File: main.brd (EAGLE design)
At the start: 78 x 235 mm, 116 parts, among them IC10 FGPMMOPA6H, IC2 25LC1024-I/P, IC6 MPL3115A2LGA, IC7 FXAS21000, IC8 ADXL343BCCZ, Q1 12MHz, Q2 MCP9700A-E/TO, Q3 FQP7P06, Q4 MCP9700A-E/TO, U1 ATMEGA1284P-PU, U2 LT3570EFEPBF, U3 TL431BQLP, X1 132134RP

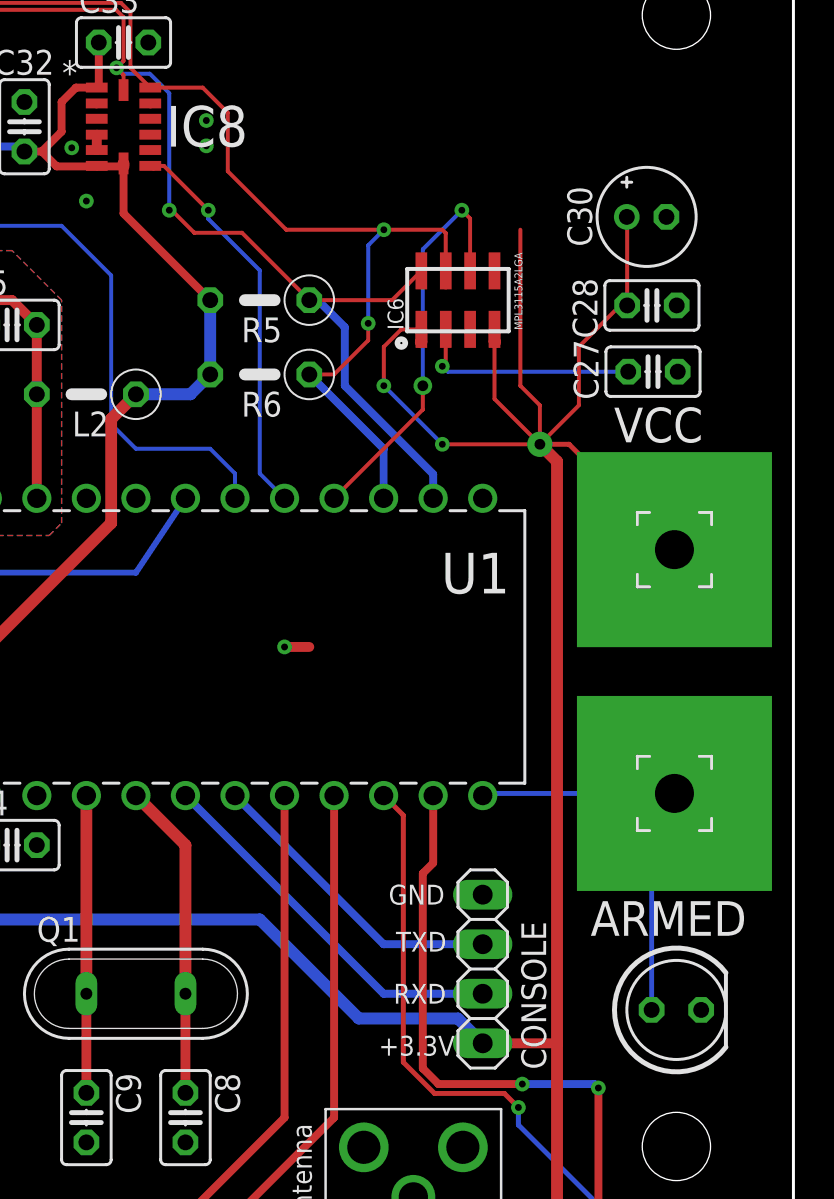
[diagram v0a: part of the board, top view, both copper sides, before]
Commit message: Changed armed sense so that the pin is pulled low when armed and added resistor for armed LED.
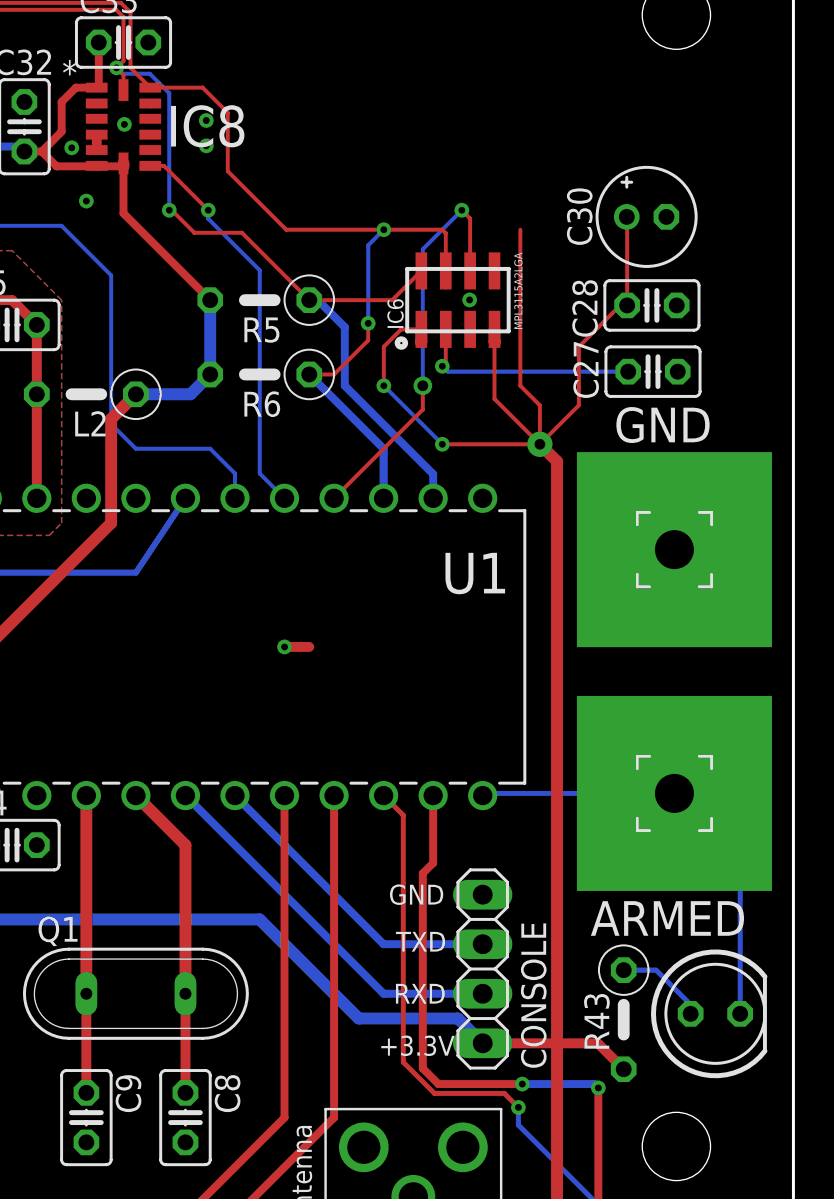
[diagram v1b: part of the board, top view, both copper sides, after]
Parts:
- added R43: 2K2Ω, rcl:0207/5V
- moved ARMED 2.01 mm to (74.0, 177.8)
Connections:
- new net N$33: ARMED.A, R43.1
- net ARMED_SENSE: now also ARMED.K; no longer ARMED.A
- net GND: now also PAD1.1; no longer ARMED.K
- net VCC: now also R43.2; no longer PAD1.1
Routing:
- net VCC: track 500.9 -> 495.7 mm
- net N$33: track 0.00 -> 4.63 mm
- net ARMED_SENSE: track 21.5 -> 22.6 mm
- net GND: vias 38 -> 40
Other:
- board text removed: "VCC"
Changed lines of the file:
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@@
 <?xml version="1.0" encoding="utf-8"?>
 <!DOCTYPE eagle SYSTEM "eagle.dtd">
-<eagle version="8.6.0">
+<eagle version="8.5.1">
 <drawing>
 <settings>
@@
 <grid distance="1" unitdist="mm" unit="mm" style="lines" multiple="1" display="no" altdistance="0.1" altunitdist="mm" altunit="mm"/>
 <layers>
-<layer number="1" name="Top" color="4" fill="1" visible="no" active="yes"/>
+<layer number="1" name="Top" color="4" fill="1" visible="yes" active="yes"/>
 <layer number="2" name="Route2" color="1" fill="3" visible="no" active="no"/>
 <layer number="3" name="Route3" color="4" fill="3" visible="no" active="no"/>
@@
 <layer number="17" name="Pads" color="2" fill="1" visible="yes" active="yes"/>
 <layer number="18" name="Vias" color="2" fill="1" visible="yes" active="yes"/>
-<layer number="19" name="Unrouted" color="6" fill="1" visible="no" active="yes"/>
-<layer number="20" name="Dimension" color="24" fill="1" visible="no" active="yes"/>
-<layer number="21" name="tPlace" color="7" fill="1" visible="no" active="yes"/>
-<layer number="22" name="bPlace" color="7" fill="1" visible="no" active="yes"/>
-<layer number="23" name="tOrigins" color="15" fill="1" visible="no" active="yes"/>
-<layer number="24" name="bOrigins" color="15" fill="1" visible="no" active="yes"/>
-<layer number="25" name="tNames" color="7" fill="1" visible="no" active="yes"/>
-<layer number="26" name="bNames" color="7" fill="1" visible="no" active="yes"/>
+<layer number="19" name="Unrouted" color="6" fill="1" visible="yes" active="yes"/>
+<layer number="20" name="Dimension" color="24" fill="1" visible="yes" active="yes"/>
+<layer number="21" name="tPlace" color="7" fill="1" visible="yes" active="yes"/>
+<layer number="22" name="bPlace" color="7" fill="1" visible="yes" active="yes"/>
+<layer number="23" name="tOrigins" color="15" fill="1" visible="yes" active="yes"/>
+<layer number="24" name="bOrigins" color="15" fill="1" visible="yes" active="yes"/>
+<layer number="25" name="tNames" color="7" fill="1" visible="yes" active="yes"/>
+<layer number="26" name="bNames" color="7" fill="1" visible="yes" active="yes"/>
 <layer number="27" name="tValues" color="7" fill="1" visible="no" active="yes"/>
 <layer number="28" name="bValues" color="7" fill="1" visible="no" active="yes"/>
@@
 <layer number="37" name="tTest" color="7" fill="1" visible="no" active="yes"/>
 <layer number="38" name="bTest" color="7" fill="1" visible="no" active="yes"/>
-<layer number="39" name="tKeepout" color="4" fill="11" visible="no" active="yes"/>
-<layer number="40" name="bKeepout" color="1" fill="11" visible="no" active="yes"/>
+<layer number="39" name="tKeepout" color="4" fill="11" visible="yes" active="yes"/>
+<layer number="40" name="bKeepout" color="1" fill="11" visible="yes" active="yes"/>
 <layer number="41" name="tRestrict" color="4" fill="10" visible="yes" active="yes"/>
-<layer number="42" name="bRestrict" color="1" fill="10" visible="no" active="yes"/>
+<layer number="42" name="bRestrict" color="1" fill="10" visible="yes" active="yes"/>
 <layer number="43" name="vRestrict" color="2" fill="10" visible="no" active="yes"/>
-<layer number="44" name="Drills" color="7" fill="1" visible="no" active="yes"/>
-<layer number="45" name="Holes" color="7" fill="1" visible="no" active="yes"/>
+<layer number="44" name="Drills" color="7" fill="1" visible="yes" active="yes"/>
+<layer number="45" name="Holes" color="7" fill="1" visible="yes" active="yes"/>
 <layer number="46" name="Milling" color="3" fill="1" visible="no" active="yes"/>
 <layer number="47" name="Measures" color="7" fill="1" visible="no" active="yes"/>
@@
 <layer number="49" name="Reference" color="7" fill="1" visible="no" active="yes"/>
 <layer number="50" name="dxf" color="7" fill="1" visible="no" active="no"/>
-<layer number="51" name="tDocu" color="7" fill="1" visible="no" active="yes"/>
-<layer number="52" name="bDocu" color="7" fill="1" visible="no" active="yes"/>
+<layer number="51" name="tDocu" color="7" fill="1" visible="yes" active="yes"/>
+<layer number="52" name="bDocu" color="7" fill="1" visible="yes" active="yes"/>
 <layer number="53" name="tGND_GNDA" color="7" fill="9" visible="no" active="no"/>
 <layer number="54" name="bGND_GNDA" color="1" fill="9" visible="no" active="no"/>
@@
 <text x="76" y="121" size="1.778" layer="21" rot="R90">SAMUEL DEWAN</text>
 <text x="67.6" y="181.8" size="1.778" layer="21">ARMED</text>
-<text x="68.8" y="207.1" size="1.778" layer="21">VCC</text>
+<text x="68.8" y="207.1" size="1.778" layer="21">GND</text>
 <text x="71" y="63" size="1.778" layer="21">+</text>
 <text x="71.6" y="37" size="1.778" layer="21">-</text>
@@
 <attribute name="VALUE" x="71.9" y="190.3" size="0.0254" layer="27"/>
 </element>
-<element name="ARMED" library="led" library_urn="urn:adsk.eagle:library:259" package="LED5MM" package3d_urn="urn:adsk.eagle:package:15799/2" value="" x="72" y="178" smashed="yes">
-<attribute name="VALUE" x="75.2004" y="176.1966" size="1.27" layer="27" ratio="10"/>
+<element name="ARMED" library="led" library_urn="urn:adsk.eagle:library:259" package="LED5MM" package3d_urn="urn:adsk.eagle:package:15799/2" value="" x="74" y="177.8" smashed="yes">
+<attribute name="VALUE" x="77.2004" y="175.9966" size="1.27" layer="27" ratio="10"/>
+</element>
+<element name="R43" library="rcl" library_urn="urn:adsk.eagle:library:334" package="0207/5V" package3d_urn="urn:adsk.eagle:package:23502/1" value="2K2Ω" x="69.3" y="177.5" smashed="yes" rot="R270">
+<attribute name="NAME" x="67.289" y="178.943" size="1.27" layer="25" ratio="10" rot="R270"/>
+<attribute name="SPICEPREFIX" value="R" x="69.3" y="177.5" size="1.778" layer="27" rot="R270" display="off"/>
+<attribute name="VALUE" x="67.141" y="178.643" size="1.27" layer="27" ratio="10" rot="R270"/>
 </element>
 </elements>
@@
 <wire x1="58" y1="65" x2="55.5694" y2="67.4306" width="0.6096" layer="1"/>
 <wire x1="55.5694" y1="67.4306" x2="55.5694" y2="67.4934" width="0.6096" layer="1"/>
-<contactref element="PAD1" pad="1"/>
-<wire x1="65" y1="207" x2="66.5" y2="207" width="0.254" layer="1"/>
-<wire x1="66.5" y1="207" x2="71.9" y2="201.6" width="0.254" layer="1"/>
+<contactref element="R43" pad="2"/>
+<wire x1="65.88" y1="176.29" x2="67.97" y2="176.29" width="0.508" layer="1"/>
+<wire x1="67.97" y1="176.29" x2="69.3" y2="174.96" width="0.508" layer="1"/>
 </signal>
 <signal name="XTAL1">
@@
 <wire x1="62.07" y1="188.99" x2="62.18" y2="189.1" width="0.254" layer="16"/>
 <wire x1="62.18" y1="189.1" x2="71.9" y2="189.1" width="0.254" layer="16"/>
-<contactref element="ARMED" pad="A"/>
-<wire x1="70.73" y1="178" x2="70.73" y2="187.93" width="0.254" layer="16"/>
-<wire x1="70.73" y1="187.93" x2="71.9" y2="189.1" width="0.254" layer="16"/>
+<contactref element="ARMED" pad="K"/>
+<wire x1="71.9" y1="189.1" x2="75.27" y2="185.73" width="0.254" layer="16"/>
+<wire x1="75.27" y1="185.73" x2="75.27" y2="177.8" width="0.254" layer="16"/>
 </signal>
 <signal name="MAIN_TRIGGER">
@@
 <via x="21.1" y="69.8" extent="1-16" drill="0.35"/>
 <via x="29.8" y="58.7" extent="1-16" drill="0.35"/>
-<contactref element="ARMED" pad="K"/>
+<via x="43.7" y="223.4" extent="1-16" drill="0.35"/>
+<via x="61.4" y="214.4" extent="1-16" drill="0.35"/>
+<contactref element="PAD1" pad="1"/>
 </signal>
 <signal name="N$73">
@@
 <contactref element="U1" pad="21"/>
 </signal>
+<signal name="N$33">
+<contactref element="R43" pad="1"/>
+<contactref element="ARMED" pad="A"/>
+<wire x1="69.3" y1="180.04" x2="70.96" y2="180.04" width="0.254" layer="16"/>
+<wire x1="72.73" y1="178.27" x2="72.73" y2="177.8" width="0.254" layer="16"/>
+<wire x1="70.96" y1="180.04" x2="72.73" y2="178.27" width="0.254" layer="16"/>
+</signal>
 </signals>

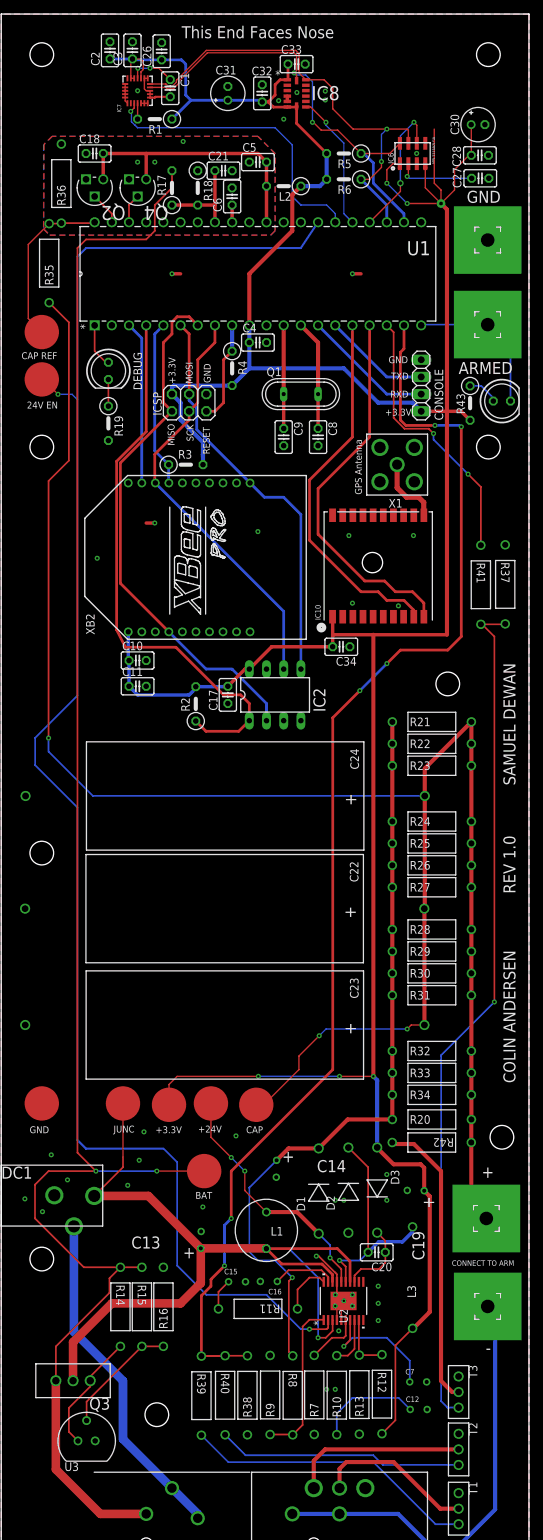
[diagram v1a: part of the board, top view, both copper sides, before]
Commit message: Fixed ERC errors and renumbered all components.
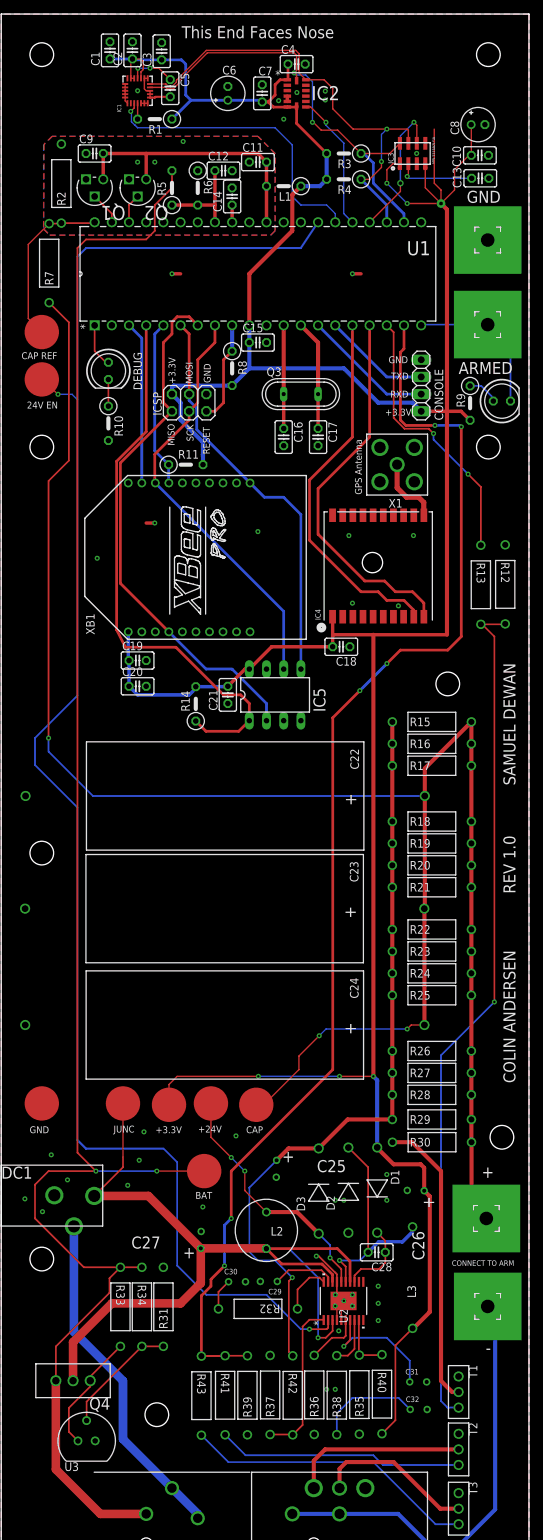
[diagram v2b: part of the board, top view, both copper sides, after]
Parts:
- removed C33, C34: 0.1µF, rcl:C025-025X050
- removed IC8: ADXL343BCCZ, CU in Space:LGA14R80P1X6_300X500X100
- removed U$10, U$9: TEST, Power:TEST
- added C25: 22µF, Power:2.5MM_AL_CAP
- added C29: 10nF, Power:2.5MM_CAP
- added IC5: 25LC1024-I/P, microchip:DIL8
- added U$7: CAP, Power:TEST
- added U$8: BAT+, Power:TEST
- ARMED: value (none) -> RED
- C10: value 47pF -> 0.1µF
- C11: value 1µF -> 0.1µF
- C12: value 1nF -> 0.1µF; device Power:2.5MM_CAP -> rcl:C025-025X050
- C13, C14: value 22µF -> 0.1µF; device Power:2.5MM_AL_CAP -> rcl:C025-025X050
- C15: value 1nF -> 2.2µF; device Power:2.5MM_CAP -> rcl:C025-025X050
- C16: value 10nF -> 27pF; device Power:2.5MM_CAP -> rcl:C025-025X050
- C17: value 0.1µF -> 27pF
- C19: value 22µF -> 47pF; device Power:2.5MM_AL_CAP -> rcl:C025-025X050
- C20: value 0.1µF -> 1µF
- C26, C27: value 0.1µF -> 22µF; device rcl:C025-025X050 -> Power:2.5MM_AL_CAP
- C30: value 10µF -> 1nF; device rcl:E2-5 -> Power:2.5MM_CAP
- C31: value 10µF -> 10nF; device rcl:E2-5 -> Power:2.5MM_CAP
- C32: value 0.1µF -> 1nF; device rcl:C025-025X050 -> Power:2.5MM_CAP
- C4: value 2.2µF -> 0.1µF
- C6: value 0.1µF -> 10µF; device rcl:C025-025X050 -> rcl:E2-5
- C7: value 10nF -> 0.1µF; device Power:2.5MM_CAP -> rcl:C025-025X050
- C8: value 27pF -> 10µF; device rcl:C025-025X050 -> rcl:E2-5
- C9: value 27pF -> 0.1µF
- IC2: value 25LC1024-I/P -> ADXL343BCCZ; device microchip:DIL8 -> CU in Space:LGA14R80P1X6_300X500X100
- L1: value 18µH -> 10µH; device Power:5.4MM_L -> rcl:0207/5V
- L2: value 10µH -> 18µH; device rcl:0207/5V -> Power:5.4MM_L
- Q1: value 12MHz -> MCP9700A-E/TO; device special:QS -> CU in Space:TO127P254X533-3
- Q3: value FQP7P06 -> 12MHz; device Power:PMOS -> special:QS
- Q4: value MCP9700A-E/TO -> FQP7P06; device CU in Space:TO127P254X533-3 -> Power:PMOS
- R10: value 24.9kΩ -> 2K2Ω; device Power:YAG_MF25 -> rcl:0207/5V
- R11: value 24.9kΩ -> 1MΩ; device Power:YAG_MF25 -> rcl:0207/5V
- R12: value 51.1kΩ -> 1M
- R13: value 17.4kΩ -> 3.6k
- R14: value 3.65kΩ -> 1MΩ; device Power:YAG_MF25 -> rcl:0207/5V
- R15, R16: value 51.1kΩ -> 750
- R17, R18: value 47kΩ -> 750; device rcl:0207/5V -> Power:YAG_MF25
- R19: value 2K2Ω -> 750; device rcl:0207/5V -> Power:YAG_MF25
- R2: value 1MΩ -> (none); device rcl:0207/5V -> Power:YAG_MF25
- R3: value 1MΩ -> 4k7Ω
- R30: value 750 -> ~1.4k
- R31, R34: value 750 -> 51.1kΩ
- R32: value 750 -> 24.9kΩ
- R33: value 750 -> 3.65kΩ
- R35: value (none) -> 17.4kΩ
- R36: value (none) -> 8.06kΩ
- R37: value 1M -> 3.65kΩ
- R38: value 1M -> 24.9kΩ
- R39: value 3.6k -> 1M
- R4: value 10kΩ -> 4k7Ω
- R40: value 3.6k -> 51.1kΩ
- R42: value ~1.4k -> 51.1kΩ
- R43: value 2K2Ω -> 3.6k; device rcl:0207/5V -> Power:YAG_MF25
- R5, R6: value 4k7Ω -> 47kΩ
- R7: value 8.06kΩ -> (none)
- R8: value 51.1kΩ -> 10kΩ; device Power:YAG_MF25 -> rcl:0207/5V
- R9: value 3.65kΩ -> 2K2Ω; device Power:YAG_MF25 -> rcl:0207/5V
- U$1: value +3.3V -> TEST
- U$2: value +24V -> TEST
- U$3: value BAT+ -> CAP
- U$4: value CAP -> BAT+
- U$5: value CAP -> +24V
- U$6: value BAT+ -> +3.3V
- moved C32 196.9 mm to (59.7, 27.5), turned to 0 degrees
- moved C31 193.5 mm to (59.6, 31.5), turned to 0 degrees
- moved C7 192.9 mm to (38.6, 223.3), turned to 90 degrees
- moved C12 186.3 mm to (32.9, 211.8)
- moved R36 182.9 mm to (46.3, 36.8)
- moved C30 176.4 mm to (32.9, 46.3)
- moved Q4 175.2 mm to (10.6, 33.0)
- moved R35 173.4 mm to (52.9, 36.8)
- moved C26 172.5 mm to (61.3, 61.1), turned to 270 degrees
- moved R7 171.8 mm to (7.09, 204.0)
- moved C28 162.8 mm to (55.5, 52.0), turned to 180 degrees
- moved C13 162.2 mm to (70.8, 210.7), turned to 0 degrees
- moved C27 162.2 mm to (29.6, 53.8), turned to 180 degrees
- moved R8 157.9 mm to (34.1, 182.6)
- moved R43 157.6 mm to (29.6, 25.0)
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- renumbered IC10 to IC4, IC6 to IC3, IC7 to IC1, PAD6 to PAD4, XB2 to XB1
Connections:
- removed net ENGINE_VALVE: U1.21
- removed net N$75: R42.2, T3.2
- new net N$34: R30.1, T1.2
- net +12.0: now also C25.1, D3.1, R15.1, R16.1, R17.1, R18.1, R19.1, R42.1; no longer C14.1, D1.1, R30.1, R31.1, R32.1, R33.1, R34.1, R8.1
- net 12V_ENABLE: now also U$2.P$1; no longer U$10.P$1
- net ACCEL_INT: now also IC2.8; no longer IC8.8
- net AREF: now also C14.1; no longer C6.1
- net ARMED_SENSE: now also PAD2.1; no longer PAD3.1
- net AVCC: now also C11.2, C9.2, L1.2, Q1.1; no longer C18.2, C5.2, L2.2, Q4.1
- net A_GND: now also C11.1, C12.2, C14.2, C9.1, Q1.3, R2.2, R6.1; no longer C18.1, C21.2, C5.1, C6.2, Q4.3, R18.1, R36.2
- net BAT+: now also Q4.3, R33.1, R34.1, R5.2, U$8.P$1; no longer Q3.3, R14.1, R15.1, R17.2, U$6.P$1
- net BAT_REF: now also C12.1, R5.1, R6.2; no longer C21.1, R17.1, R18.2
- net CAP_DISCHARGE: now also R13.1; no longer R41.1
- net CAP_REF: now also R2.1, R7.2, U$1.P$1; no longer R35.2, R36.1, U$9.P$1
- net EEPROM_CS: now also IC5.1, R14.1; no longer IC2.1, R2.1
- net FB1: now also R37.1, R42.2; no longer R8.2, R9.1
- net GND: now also C18.1, C20.2, C21.2, C25.2, C29.2, C30.2, C31.2, C5.2, C6.-, C8.-, IC2.12, IC2.2, IC2.5, IC5.3, IC5.4, IC5.7, R10.2, R12.1, R31.2, R35.1, R36.1, R37.2, R39.1, U$3.P$1; no longer C11.2, C12.2, C14.2, C28.2, C30.-, C31.-, C33.2, C34.1, C8.2, C9.2, IC2.3, IC2.7, IC8.12, IC8.2, IC8.4, IC8.5, R13.1, R16.2, R19.2, R37.1, R38.1, R7.1, R9.2, U$5.P$1
- net MAIN_TRIGGER: now also R39.2, R41.1, R43.1; no longer R38.2, R39.1, R40.1
- net MISO: now also IC5.2; no longer IC2.2
- net MOSI: now also IC5.5; no longer IC2.5
- net N$1: now also C5.1; no longer C1.1
- net N$10: now also C32.1, R38.1; no longer C12.1, R10.1
- net N$11: now also R32.1; no longer R11.1
- net N$12: now also C29.1; no longer C16.1
- net N$13: now also C28.2; no longer C20.2
- net N$15: now also R35.2, R40.1; no longer R12.1, R13.2
- net N$16: now also C28.1, D1.1; no longer C20.1, D3.1
- net N$3: now also C13.1; no longer C27.1
- net N$33: now also R9.1; no longer R43.1
- net N$5: now also C31.1; no longer C7.1
- net N$6: now also R36.2; no longer R7.2
- net N$69: now also Q4.1, R33.2; no longer Q3.1, R14.2
- net N$7: now also R38.2; no longer R10.2
- net N$70: now also R31.1, R34.2; no longer R15.2, R16.1
- net N$71: now also R10.1; no longer R19.1
- net N$77: now also T3.2; no longer T1.2
- net N$79: now also R43.2, T3.3; no longer R39.2, T1.3
- net N$8: now also D3.2, L2.2, U$5.P$1; no longer D1.2, L1.2, U$2.P$1
- net N$80: now also R41.2; no longer R40.2
- net N$81: now also PAD3.1, R15.2, R16.2, R17.2, R18.2, R19.2, R7.1, U$7.P$1; no longer PAD2.1, R31.2, R32.2, R33.2, R34.2, R35.1, R42.1, U$4.P$1
- net N$82: now also R12.2, R13.2, T1.3; no longer R37.2, R41.2, T3.3
- net N$9: now also C30.1, R32.2; no longer C15.1, R11.2
- net PWR_JUNC: now also C27.1, L2.1, Q4.2, U$4.P$1; no longer C13.1, L1.1, Q3.2, U$3.P$1
- net RADIO_CS: now also R11.1; no longer R3.1
- net RESET: now also R8.1; no longer R4.1
- net SCK: now also IC5.6; no longer IC2.6
- net SCL: now also IC2.14, R3.1; no longer IC8.14, R5.1
- net SDA: now also IC2.13, R4.1; no longer IC8.13, R6.1
- net TEMP: now also Q1.2; no longer Q2.2
- net TEMP2: now also Q2.2; no longer Q4.2
- net VCC: now also C1.1, C15.1, C18.2, C20.1, C21.1, C6.+, C7.1, C8.+, D1.2, IC2.1, IC2.6, IC2.7, IC5.8, L1.1, R11.2, R14.2, R40.2, R8.2, R9.2, U$6.P$1; no longer C11.1, C17.1, C28.1, C30.+, C31.+, C32.1, C33.1, C34.2, D3.2, IC2.8, IC8.1, IC8.6, IC8.7, L2.1, R12.2, R2.2, R43.2, R5.2, R6.2, U$1.P$1
- net XTAL1: now also C17.1, Q3.2; no longer C8.1, Q1.2
- net XTAL2: now also C16.1, Q3.1; no longer C9.1, Q1.1
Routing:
- net N$75: track 43.3 -> 0.00 mm
- net N$34: track 0.00 -> 43.2 mm
- net N$81: track 280.0 -> 280.6 mm
